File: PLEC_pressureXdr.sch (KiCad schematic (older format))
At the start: 3 parts, among them U7 NBPMANN150

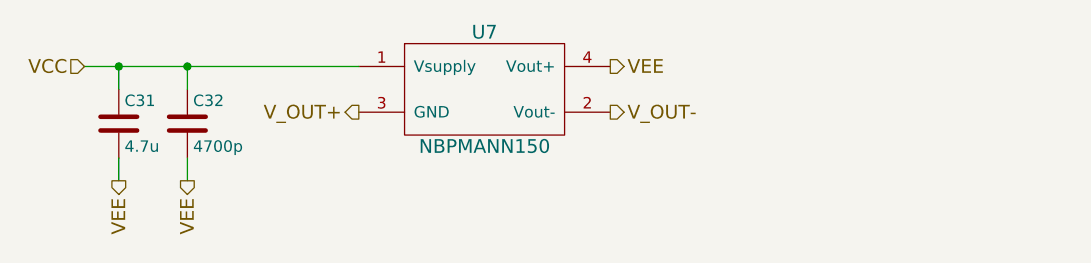
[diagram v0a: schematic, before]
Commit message: Almost done with layout; need to rearrange uC pins
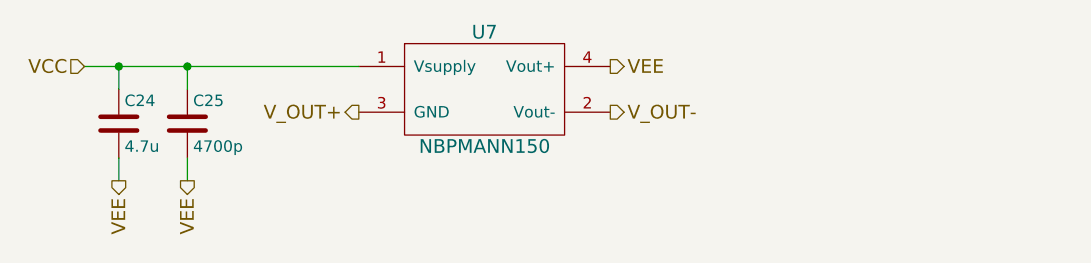
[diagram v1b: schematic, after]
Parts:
- renumbered C31 to C24, C32 to C25
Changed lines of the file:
@@
 V_OUT+
 $Comp
-L C C31
+L C C24
 U 1 1 5A76BF8A
 P 4350 3900
-F 0 "C31" H 4375 4000 50  0000 L CNN
+F 0 "C24" H 4375 4000 50  0000 L CNN
 F 1 "4.7u" H 4375 3800 50  0000 L CNN
 F 2 "PLEC:THTm_1.5Px4Dx7H_4.7u" H 4388 3750 50  0001 C CNN
@@
 Connection ~ 4350 3650
 $Comp
-L C C32
+L C C25
 U 1 1 5A75A0B3
 P 4650 3900
-F 0 "C32" H 4675 4000 50  0000 L CNN
+F 0 "C25" H 4675 4000 50  0000 L CNN
 F 1 "4700p" H 4675 3800 50  0000 L CNN
 F 2 "PLEC:THTt_100Px150Lx100Wx183H_4700p" H 4688 3750 50  0001 C CNN

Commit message: Replaced solid state relays with NPN Darlingtons
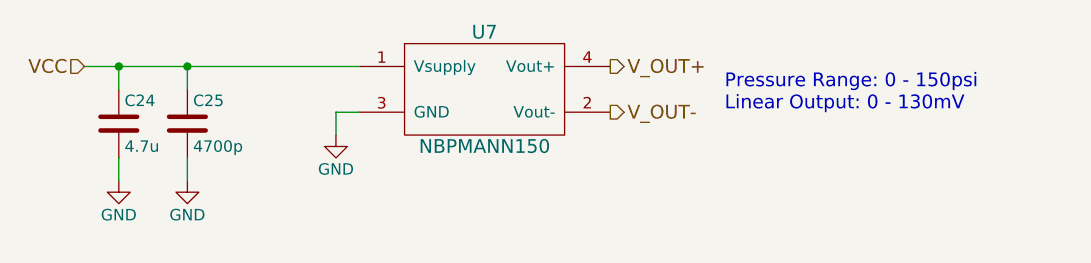
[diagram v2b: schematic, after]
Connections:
- net V_OUT+: now also U7.4 (Vout+); no longer U7.3 (GND)
- net VEE renamed GND
- net GND: now also U7.3 (GND); no longer U7.4 (Vout+)
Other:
- note added: "Pressure Range: 0 - 150psi\nLinear Output: 0 - 130mV"
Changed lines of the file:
@@
 EESchema Schematic File Version 2
+LIBS:PLEC-rescue
 LIBS:power
 LIBS:device
@@
 LIBS:PLEC
 LIBS:cap_470u
+LIBS:BDW42G
 LIBS:PLEC-cache
 EELAYER 25 0
@@
 Text HLabel 4200 3650 0    60   Input ~ 0
 VCC
-Text HLabel 6500 3650 2    60   Output ~ 0
-VEE
 Text HLabel 6500 3850 2    60   Output ~ 0
 V_OUT-
-Text HLabel 5400 3850 0    60   Output ~ 0
+Text HLabel 6500 3650 2    60   Output ~ 0
 V_OUT+
 $Comp
@@
 Wire Wire Line
 	4200 3650 5400 3650
-Text HLabel 4350 4150 3    60   Output ~ 0
-VEE
 Connection ~ 4350 3650
 $Comp
@@
 Wire Wire Line
 	4650 4050 4650 4150
-Text HLabel 4650 4150 3    60   Output ~ 0
-VEE
 Wire Wire Line
 	4650 3750 4650 3650
 Connection ~ 4650 3650
+$Comp
+L GND #PWR032
+U 1 1 5A84AF98
+P 4350 4150
+F 0 "#PWR032" H 4350 3900 50  0001 C CNN
+F 1 "GND" H 4350 4000 50  0000 C CNN
+F 2 "" H 4350 4150 50  0001 C CNN
+F 3 "" H 4350 4150 50  0001 C CNN
+	1    4350 4150
+	1    0    0    -1
+$EndComp
+$Comp
+L GND #PWR033
+U 1 1 5A84AFD5
+P 4650 4150
+F 0 "#PWR033" H 4650 3900 50  0001 C CNN
+F 1 "GND" H 4650 4000 50  0000 C CNN
+F 2 "" H 4650 4150 50  0001 C CNN
+F 3 "" H 4650 4150 50  0001 C CNN
+	1    4650 4150
+	1    0    0    -1
+$EndComp
+$Comp
+L GND #PWR034
+U 1 1 5A84B5B8
+P 5300 3950
+F 0 "#PWR034" H 5300 3700 50  0001 C CNN
+F 1 "GND" H 5300 3800 50  0000 C CNN
+F 2 "" H 5300 3950 50  0001 C CNN
+F 3 "" H 5300 3950 50  0001 C CNN
+	1    5300 3950
+	1    0    0    -1
+$EndComp
+Wire Wire Line
+	5300 3850 5300 3950
+Wire Wire Line
+	5300 3850 5400 3850
+Text Notes 7000 3850 0    60   ~ 0
+Pressure Range: 0 - 150psi\nLinear Output: 0 - 130mV
 $EndSCHEMATC
